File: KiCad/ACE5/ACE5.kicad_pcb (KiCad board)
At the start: 2 copper layers, 160 x 100 mm, 90 parts, among them IC1 LM7805_TO220, IC10 74LS273, IC4 74LS04, IC5 74LS02, IC7 74LS365, IC8 74LS30, IC9 74LS365, Q1 2N3904, Q2 5MHz, Q3 BC237, U1 74LS138, X2 CRYSTALHC49U-V 6.556MHz

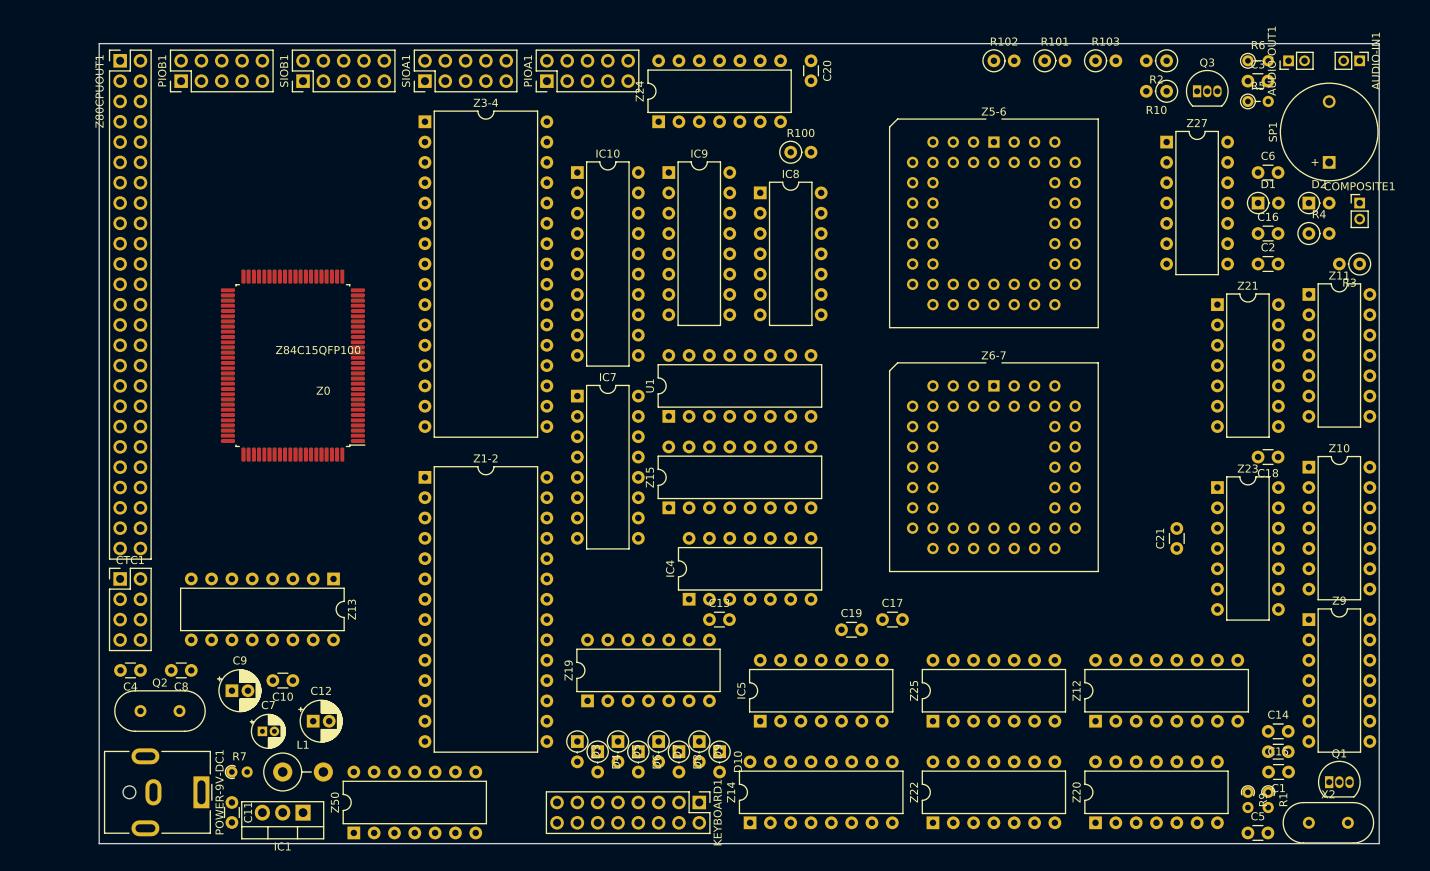
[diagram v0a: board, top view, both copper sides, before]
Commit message: Update numbering. Change footprints.
Signed-off-by: John Bradley <flypie@rocketmail.com>
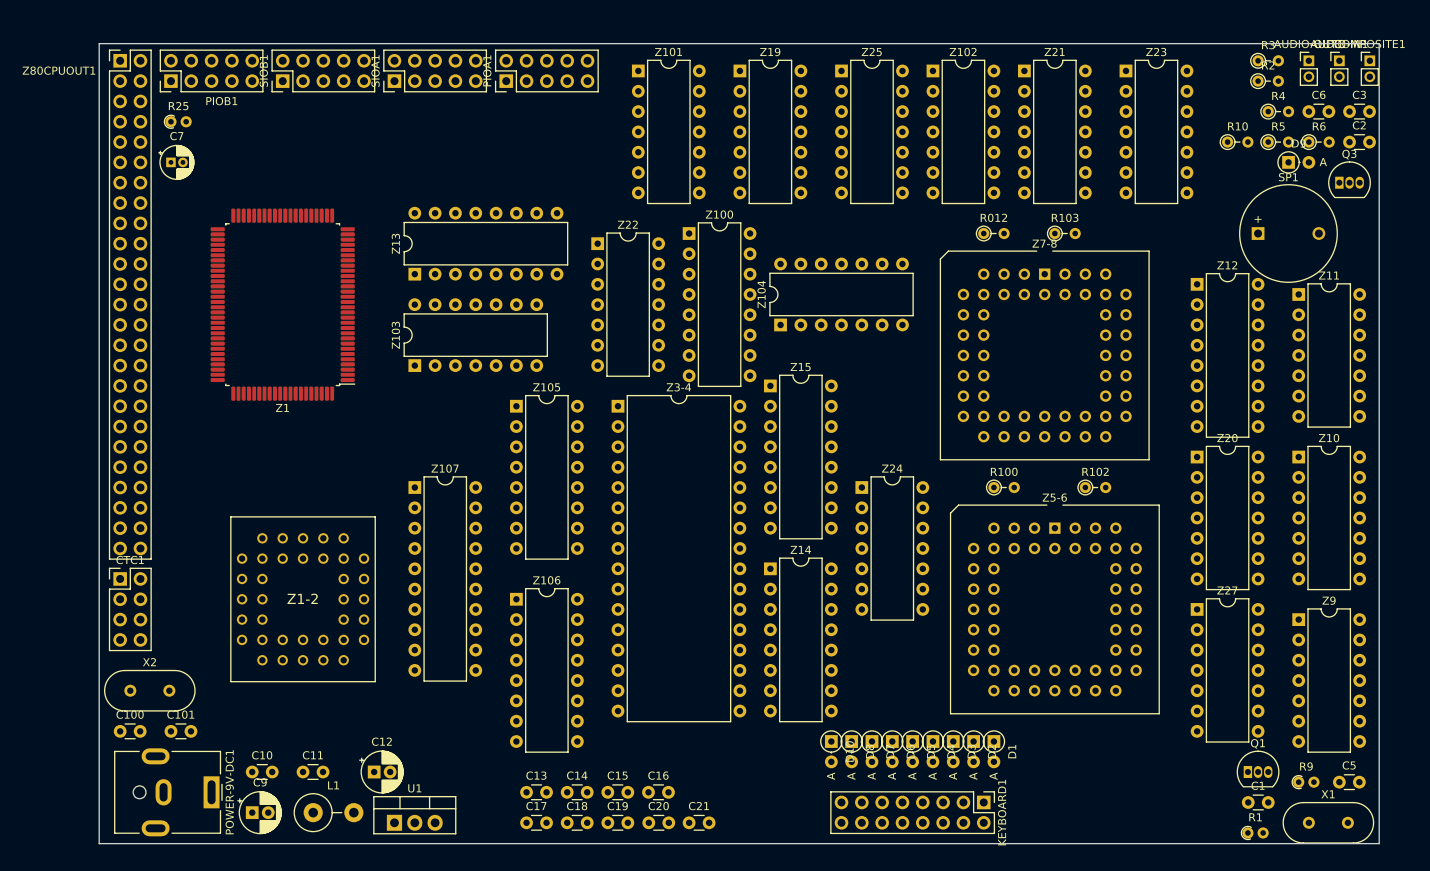
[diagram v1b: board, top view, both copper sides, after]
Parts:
- removed C4: 22p, Capacitor_THT:C_Disc_D3.0mm_W1.6mm_P2.50mm
- removed C8: 42p, Capacitor_THT:C_Disc_D3.0mm_W1.6mm_P2.50mm
- removed IC1: LM7805_TO220, Package_TO_SOT_THT:TO-220-3_Vertical
- removed IC10: 74LS273, Package_DIP:DIP-20_W7.62mm
- removed IC4: 74LS04, Package_DIP:DIP-14_W7.62mm
- removed IC5: 74LS02, Package_DIP:DIP-14_W7.62mm
- removed IC7, IC9: 74LS365, Package_DIP:DIP-16_W7.62mm
- removed IC8: 74LS30, Package_DIP:DIP-14_W7.62mm
- removed Q2: 5MHz, Crystal:Crystal_HC49-U_Vertical
- removed R101: R, Resistor_THT:R_Axial_DIN0207_L6.3mm_D2.5mm_P2.54mm_Vertical
- removed R7: 220k, Resistor_THT:R_Axial_DIN0204_L3.6mm_D1.6mm_P1.90mm_Vertical
- removed Z0: Z84C15QFP100, Package_QFP:PQFP-100_14x20mm_P0.65mm
- removed Z50: 74LS21, Package_DIP:DIP-14_W7.62mm
- removed Z6-7: 71321SA55JG8, Package_LCC:PLCC-52_THT-Socket
- added C100: 22p, Capacitor_THT:C_Disc_D3.0mm_W1.6mm_P2.50mm, F.Cu at (71.1, 141.0)
- added C101: 42p, Capacitor_THT:C_Disc_D3.0mm_W1.6mm_P2.50mm, F.Cu at (77.5, 141.0)
- added R012: R, Resistor_THT:R_Axial_DIN0204_L3.6mm_D1.6mm_P2.54mm_Vertical, F.Cu at (179.1, 78.7)
- added R25: 220k, Resistor_THT:R_Axial_DIN0204_L3.6mm_D1.6mm_P1.90mm_Vertical, F.Cu at (77.5, 64.8)
- added X1: CRYSTALHC49U-V 6.556MHz, Crystal:Crystal_HC49-U_Vertical, F.Cu at (219.7, 152.4)
- added Z1: Z84C15QFP100, Package_QFP:PQFP-100_14x20mm_P0.65mm, F.Cu at (91.4, 87.6)
- added Z100: 74HCT138, Package_DIP:DIP-16_W7.62mm, F.Cu at (142.2, 78.7)
- added Z101: 74HCT21, Package_DIP:DIP-14_W7.62mm, F.Cu at (135.9, 58.4)
- added Z102: 74HCT04, Package_DIP:DIP-14_W7.62mm, F.Cu at (172.7, 58.4)
- added Z103: 74HCT02, Package_DIP:DIP-14_W7.62mm, F.Cu at (108.0, 95.2)
- added Z104: 74HCT30, Package_DIP:DIP-14_W7.62mm, F.Cu at (153.7, 90.2)
- added Z105: 74HCT365, Package_DIP:DIP-16_W7.62mm, F.Cu at (120.7, 100.3)
- added Z106: 74HCT365, Package_DIP:DIP-16_W7.62mm, F.Cu at (120.7, 124.5)
- added Z107: 74HCT273, Package_DIP:DIP-20_W7.62mm, F.Cu at (108.0, 110.5)
- added Z7-8: 71321SA55JG8, Package_LCC:PLCC-52_THT-Socket, F.Cu at (186.7, 83.8)
- R10, R100, R102, R103, R2, R3, R4: footprint Resistor_THT:R_Axial_DIN0207_L6.3mm_D2.5mm_P2.54mm_Vertical -> Resistor_THT:R_Axial_DIN0204_L3.6mm_D1.6mm_P2.54mm_Vertical
- U1: value 74LS138 -> LM7805_TO220; footprint Package_DIP:DIP-16_W7.62mm -> Package_TO_SOT_THT:TO-220-3_Vertical
- X2: value CRYSTALHC49U-V 6.556MHz -> 5MHz
- Z1-2: footprint Package_DIP:DIP-28_W15.24mm -> Package_LCC:PLCC-32_THT_Socket_11.4x14.0mm_P1.27mm
- Z10, Z11, Z9: value 74LS393 -> 74HCT393
- Z12: value 74LS166 -> 74HCT166
- Z13: value 74LS138 -> 74HCT138
- Z14, Z15: value 74LS367 -> 74HCT367
- Z19: value 74LS00 -> 74HCT00
- Z20: value 74LS08 -> 74HCT08
- Z21, Z22: value 74LS11 -> 74HCT11
- Z23: value 74LS86 -> 74HCT86
- Z24, Z25: value 74LS02 -> 74HCT02
- Z27: value 74LS74 -> 74HCT74
- moved X2 148.2 mm to (72.4, 135.9)
- moved C16 103.4 mm to (137.2, 148.6)
- moved D9 103.3 mm to (217.2, 69.8), turned to 0 degrees
- moved C18 99.9 mm to (127.0, 152.4), turned to 0 degrees
- moved C20 97.4 mm to (137.2, 152.4), turned to 0 degrees
- moved C14 88.0 mm to (127.0, 148.6)
- moved Z22 83.6 mm to (130.8, 80.0), turned to 0 degrees
- moved C15 82.7 mm to (132.1, 148.6)
- moved Z25 82.1 mm to (161.3, 58.4), turned to 0 degrees
- moved Z19 81.0 mm to (148.6, 58.4), turned to 0 degrees
- moved D2 79.3 mm to (177.8, 142.2), turned to 270 degrees
- moved D1 75.0 mm to (180.3, 142.2), turned to 270 degrees
- moved C7 72.0 mm to (77.5, 69.8)
- moved C21 69.9 mm to (142.2, 152.4), turned to 0 degrees
- moved U1 61.3 mm to (105.4, 152.4), turned to 0 degrees
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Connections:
- C2 pad 1: Net-(AUDIO-IN1-Pad1) -> Net-(AUDIO-OUT1-Pad1)
- C3 pad 1: Net-(AUDIO-OUT1-Pad1) -> Net-(AUDIO-IN1-Pad1)
- C6 pad 1: Net-(AUDIO-IN1-Pad1) -> Net-(AUDIO-OUT1-Pad1)
- D1 pad 1: Net-(D1-Pad1) -> /A8
- D1 pad 2: Net-(COMPOSITE1-Pad1) -> Net-(D1-Pad2)
- D10 pad 1: /A8 -> Net-(D10-Pad1)
- D10 pad 2: Net-(D10-Pad2) -> Net-(COMPOSITE1-Pad1)
- D2 pad 1: Net-(D2-Pad1) -> /A9
- D2 pad 2: Net-(C2-Pad2) -> Net-(D2-Pad2)
- D3 pad 1: /A15 -> /A10
- D4 pad 1: /A14 -> /A11
- D5 pad 1: /A13 -> /A12
- D6 pad 1: /A12 -> /A13
- D7 pad 1: /A11 -> /A14
- D8 pad 1: /A10 -> /A15
- D9 pad 1: /A9 -> Net-(AUDIO-OUT1-Pad1)
- D9 pad 2: Net-(D9-Pad2) -> Net-(C2-Pad2)
- KEYBOARD1 pad 1: Net-(D10-Pad2) -> Net-(D1-Pad2)
- KEYBOARD1 pad 11: Net-(D5-Pad2) -> Net-(D6-Pad2)
- KEYBOARD1 pad 13: Net-(D4-Pad2) -> Net-(D7-Pad2)
- KEYBOARD1 pad 15: Net-(D3-Pad2) -> Net-(D8-Pad2)
- KEYBOARD1 pad 3: Net-(D9-Pad2) -> Net-(D2-Pad2)
- KEYBOARD1 pad 5: Net-(D8-Pad2) -> Net-(D3-Pad2)
- KEYBOARD1 pad 7: Net-(D7-Pad2) -> Net-(D4-Pad2)
- KEYBOARD1 pad 9: Net-(D6-Pad2) -> Net-(D5-Pad2)
- R6 pad 2: Net-(AUDIO-OUT1-Pad1) -> Net-(AUDIO-IN1-Pad1)
- SP1 pad 1: Net-(D2-Pad1) -> Net-(AUDIO-OUT1-Pad1)
- U1 pad 1: /A11 -> +9V
- U1 pad 2: /A12 -> GND
- U1 pad 3: GND -> +5V
- X2 pad 1: Net-(C1-Pad1) -> Net-(C100-Pad2)
- X2 pad 2: Net-(C5-Pad2) -> Net-(C101-Pad2)
- Z1-2 pad 10: /A0 -> /A1
- Z1-2 pad 11: /DA0 -> /A0
- Z1-2 pad 12: /DA1 -> Net-(Z1-2-Pad12)
- Z1-2 pad 13: /DA2 -> /DA0
- Z1-2 pad 14: GND -> /DA1
- Z1-2 pad 15: /DA3 -> /DA2
- Z1-2 pad 16: /DA4 -> Net-(Z1-2-Pad16)
- Z1-2 pad 17: /DA5 -> Net-(Z1-2-Pad17)
- Z1-2 pad 18: /DA6 -> /DA3
- Z1-2 pad 19: /DA7 -> /DA4
- Z1-2 pad 2: /A12 -> /A15
- Z1-2 pad 20: Net-(Z1-2-Pad20) -> /DA5
- Z1-2 pad 21: /A10 -> /DA6
- Z1-2 pad 22: Net-(Z1-2-Pad20) -> /DA7
- Z1-2 pad 23: /A11 -> Net-(Z1-2-Pad23)
- Z1-2 pad 24: /A9 -> /A10
- Z1-2 pad 25: /A8 -> Net-(Z1-2-Pad23)
- Z1-2 pad 26: /A13 -> Net-(Z1-2-Pad26)
- Z1-2 pad 27: /A14 -> /A11
- Z1-2 pad 28: +5V -> /A9
- Z1-2 pad 3: /A7 -> /A12
- Z1-2 pad 4: /A6 -> /A7
- Z1-2 pad 5: /A5 -> /A6
- Z1-2 pad 6: /A4 -> /A5
- Z1-2 pad 7: /A3 -> /A4
- Z1-2 pad 8: /A2 -> /A3
- Z1-2 pad 9: /A1 -> /A2
- Z13 pad 14: Net-(U1-Pad4) -> Net-(Z100-Pad4)
- Z23 pad 4: Net-(Z23-Pad4) -> (no net)
- Z23 pad 5: Net-(Z23-Pad5) -> (no net)
- Z23 pad 6: Net-(Z23-Pad6) -> (no net)
- Z25 pad 10: (no net) -> /IOREQ&11111111B
- Z25 pad 4: Net-(D1-Pad1) -> Net-(D10-Pad1)
- Z25 pad 8: (no net) -> Net-(Z103-Pad6)
- Z25 pad 9: (no net) -> Net-(Z102-Pad4)
- Z5-6 pad 1: Net-(U1-Pad13) -> Net-(Z100-Pad13)
- Z5-6 pad 49: Net-(R101-Pad2) -> Net-(R102-Pad2)

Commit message: UPdate to latest version.
Signed-off-by: John Bradley <flypie@rocketmail.com>
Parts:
- added D100: BAT54W, Package_TO_SOT_SMD:SOT-323_SC-70, F.Cu at (130.9, 91.8)
- added HBL1: MountingHole, MountingHole:MountingHole_2.5mm, F.Cu at (236.0, 138.0)
- added HBR1: MountingHole, MountingHole:MountingHole_2.5mm, F.Cu at (106.0, 138.0)
- added HTL1: MountingHole, MountingHole:MountingHole_2.5mm, F.Cu at (106.0, 58.0)
- added HTR1: MountingHole, MountingHole:MountingHole_2.5mm, F.Cu at (236.0, 58.0)
- L1: value L -> 100 nH
- POWER-9V-DC1: value Conn_01x02 -> PJ-036C; footprint Connector_BarrelJack:BarrelJack_CUI_PJ-063AH_Horizontal -> cuipj:CUI_PJ-036C
- moved Z27 68.7 mm to (215.5, 57.8), turned to 90 degrees
- moved Z24 65.8 mm to (229.5, 106.0)
- moved Z22 46.0 mm to (171.1, 57.8), turned to 90 degrees
- moved Z19 45.4 mm to (193.9, 57.8), turned to 90 degrees
- moved R101 40.0 mm to (201.6, 71.7)
- moved Z20 37.5 mm to (215.5, 70.5), turned to 90 degrees
- moved Z101 35.2 mm to (154.6, 88.2), turned to 90 degrees
- moved R100 34.6 mm to (214.3, 103.5)
- moved R10 33.7 mm to (242.3, 59.5)
- moved R5 33.6 mm to (247.3, 59.3)
- moved R102 32.2 mm to (210.5, 71.7)
- moved D9 30.2 mm to (247.3, 69.8)
- moved Z15 29.2 mm to (180.0, 88.2)
- moved R25 29.0 mm to (106.4, 62.5), turned to 180 degrees
- moved R103 28.9 mm to (202.8, 103.5)
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- renumbered R102 to R101, R012 to R102, Z1 to Z0
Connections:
- Z1-2 pad 16: Net-(Z1-2-Pad16) -> GND
- Z102 pad 8: //INT -> Net-(D100-Pad3)
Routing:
- net GND: track 0.00 -> 947.6 mm, vias 0 -> 2
- net +5V: track 0.00 -> 789.6 mm, vias 0 -> 4
- net /DA7: track 0.00 -> 410.8 mm, vias 0 -> 2
- net /DA0: track 0.00 -> 323.2 mm, vias 0 -> 4
- net /DA6: track 0.00 -> 309.5 mm, vias 0 -> 4
- net /A1: track 0.00 -> 293.2 mm, vias 0 -> 2
- net /A4: track 0.00 -> 280.4 mm, vias 0 -> 2
- net /A2: track 0.00 -> 279.4 mm, vias 0 -> 3
- net /A6: track 0.00 -> 267.9 mm, vias 0 -> 5
- net /A0: track 0.00 -> 266.7 mm, vias 0 -> 3
- net /A7: track 0.00 -> 261.7 mm, vias 0 -> 3
- net /A10: track 0.00 -> 252.7 mm, vias 0 -> 6
- net /DA2: track 0.00 -> 250.5 mm, vias 0 -> 4
- net //WR: track 0.00 -> 250.4 mm, vias 0 -> 3
- net /DA3: track 0.00 -> 244.1 mm, vias 0 -> 1
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
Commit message: Update and realign schematics. Change mount of some components.
Signed-off-by: John Bradley <flypie@rocketmail.com>
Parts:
- added R104: R, Resistor_THT:R_Axial_DIN0204_L3.6mm_D1.6mm_P2.54mm_Vertical, F.Cu at (126.4, 55.2)
- added R105: R, Resistor_THT:R_Axial_DIN0204_L3.6mm_D1.6mm_P2.54mm_Vertical, F.Cu at (113.0, 55.2)
- added R106: R, Resistor_THT:R_Axial_DIN0204_L3.6mm_D1.6mm_P2.54mm_Vertical, F.Cu at (125.7, 24.1)
- added R107: R, Resistor_THT:R_Axial_DIN0204_L3.6mm_D1.6mm_P2.54mm_Vertical, F.Cu at (110.5, 24.1)
- AUDIO-IN1, AUDIO-OUT1, COMPOSITE1: footprint Connector_PinHeader_2.00mm:PinHeader_1x02_P2.00mm_Vertical -> Connector_PinHeader_2.54mm:PinHeader_1x02_P2.54mm_Vertical
- C11: value 100nf -> 100uf; footprint Capacitor_THT:C_Disc_D3.0mm_W1.6mm_P2.50mm -> Capacitor_THT:CP_Radial_D4.0mm_P1.50mm
- moved C14 168.8 mm to (41.3, 12.1), turned to 270 degrees
- moved C13 159.1 mm to (64.5, 4.00), turned to 90 degrees
- moved C18 146.2 mm to (99.5, 8.00), turned to 90 degrees
- moved C16 144.5 mm to (41.9, 57.8)
- moved KEYBOARD1 130.6 mm to (80.0, 95.0)
- moved D6 130.1 mm to (68.6, 88.7)
- moved D1 130.1 mm to (81.3, 88.7)
- moved D10 130.1 mm to (61.0, 88.7)
- moved D2 130.1 mm to (78.8, 88.7)
- moved D3 130.1 mm to (76.3, 88.7)
- moved D4 130.1 mm to (73.7, 88.7)
- moved D5 130.1 mm to (71.2, 88.7)
- moved D7 130.1 mm to (66.1, 88.7)
- moved D8 130.1 mm to (63.6, 88.7)
- moved R5 118.5 mm to (142.0, 5.00)
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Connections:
- net //INT renamed #INT
- net Net-(COMPOSITE1-Pad1) renamed /VIDEO
- C12 pad 1: GND -> +5V
- C12 pad 2: +5V -> GND
- C9 pad 1: GND -> +9V
- C9 pad 2: +9V -> GND
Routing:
- net /DA7: track 410.8 -> 250.0 mm, vias 2 -> 5
- net #CPUCLK: track 184.3 -> 312.4 mm, vias 3 -> 2
- net /A8: track 201.6 -> 298.0 mm, vias 4 -> 3
- net //MREQ: track 141.5 -> 227.8 mm, vias 1 -> 2
- net /A9: track 204.8 -> 286.0 mm, vias 5 -> 4
- net Net-(Z22-Pad2): track 23.0 -> 102.2 mm
- net +5V: track 789.6 -> 867.4 mm
- net /CNT1: track 122.7 -> 47.8 mm, vias 2 -> 0
- net /VIDEN: track 56.2 -> 130.3 mm, vias 0 -> 2
- net /CNT2: track 121.2 -> 49.6 mm, vias 1 -> 0
- net /CNT0: track 115.7 -> 45.4 mm, vias 1 -> 0
- net Net-(Z13-Pad9): track 44.3 -> 103.6 mm
- net Net-(R101-Pad2): track 51.8 -> 5.62 mm, vias 2 -> 0
- net /#PAGED8K: track 98.6 -> 144.4 mm, vias 0 -> 1
- net /A6: track 267.9 -> 224.9 mm, vias 5 -> 3
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
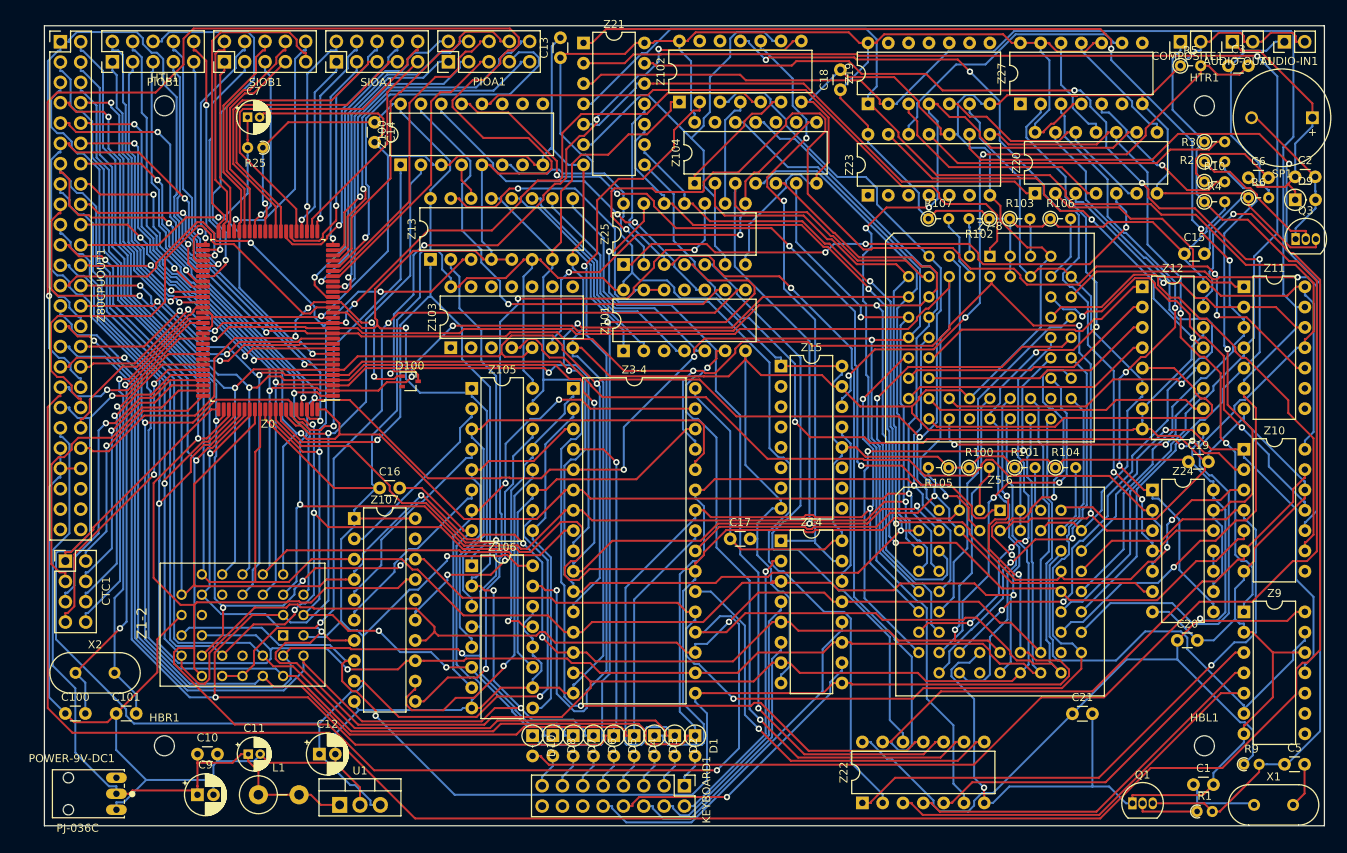
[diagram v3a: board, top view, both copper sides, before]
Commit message: Correct all routing.
Signed-off-by: John Bradley <flypie@rocketmail.com>
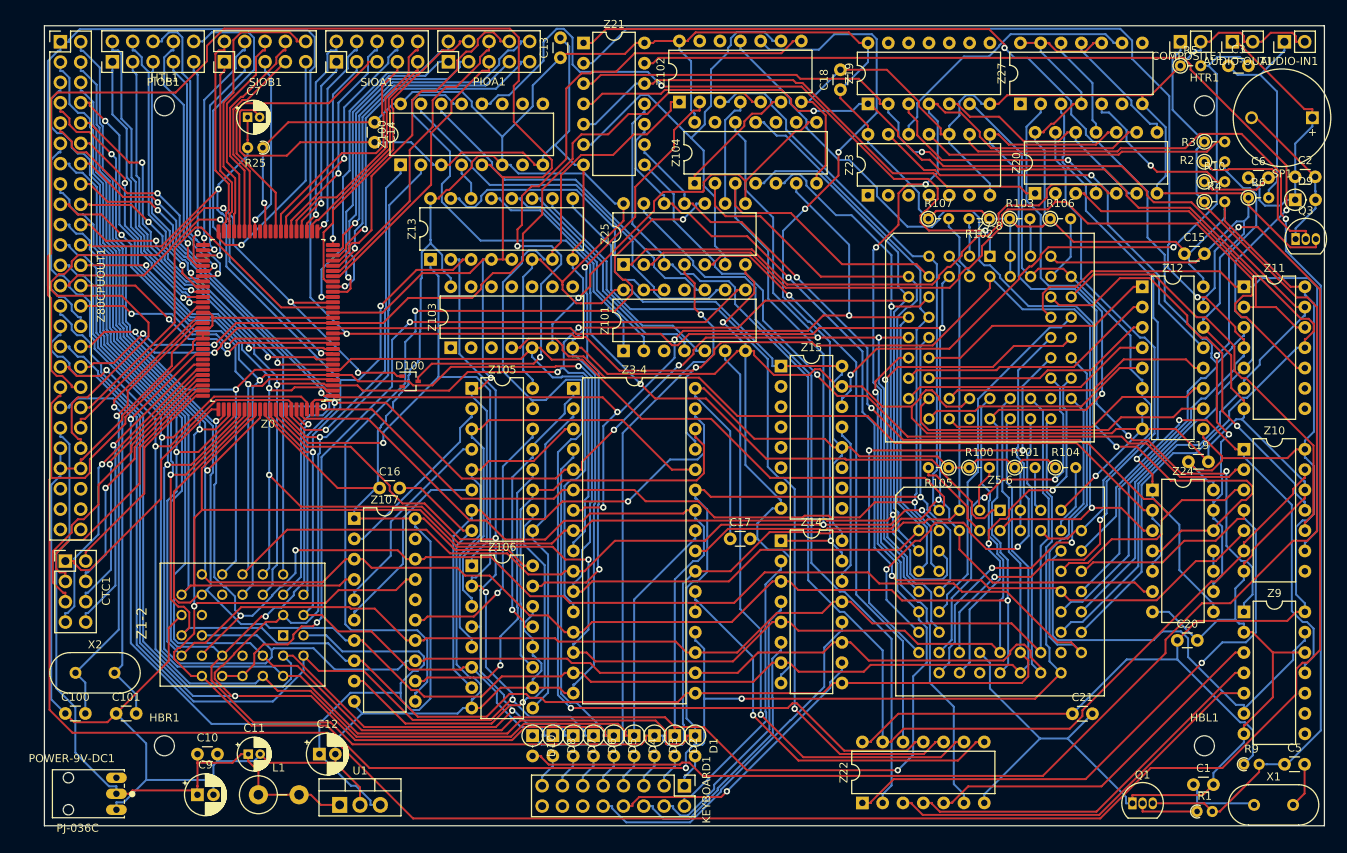
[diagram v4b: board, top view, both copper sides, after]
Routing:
- net /ENDOFSCR: track 152.5 -> 107.0 mm, vias 3 -> 0
- net #INT: track 59.9 -> 100.2 mm, vias 4 -> 3
- net /A4: track 271.0 -> 232.2 mm
- net /A8: track 298.0 -> 263.0 mm, vias 3 -> 2
- net Net-(Z102-Pad2): track 107.1 -> 74.8 mm
- net /SCREENY3: track 191.0 -> 160.8 mm
- net /DA3: track 249.8 -> 221.0 mm, vias 5 -> 1
- net /A9: track 286.0 -> 313.8 mm, vias 4 -> 2
- net /SCREENY4: track 186.9 -> 159.1 mm, vias 0 -> 1
- net /DA6: track 312.3 -> 285.9 mm, vias 2 -> 4
- net /IOREQ&11111111B: track 90.3 -> 110.2 mm, vias 3 -> 2
- net Net-(Z12-Pad5): track 48.3 -> 29.3 mm
- net /DA1: track 256.5 -> 275.0 mm, vias 4 -> 1
- net //MREQ: track 227.8 -> 209.6 mm, vias 2 -> 1
- net Net-(Z102-Pad10): track 78.6 -> 95.5 mm, vias 2 -> 3
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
